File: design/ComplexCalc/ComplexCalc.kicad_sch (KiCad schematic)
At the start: 49 parts, among them J1 V_Battery, J2 Conn_01x09, J3 STLINK, J4 Conn_01x20_Socket, J5 Conn_01x20_Socket, SW1 4, SW10 -, SW11 del, SW12 <-, SW13 7, SW14 8, SW15 9, SW16 M, SW17 SW_DPST_x2, SW18 MOD, SW19 <, SW2 5, SW20 MOD, SW22 ^, SW23 OK, SW24 v, SW26 MOD, SW27 >, SW28 MOD, SW3 6, SW4 1, SW5 2, SW6 3, SW7 =, SW8 ., SW9 0, U2 AMS1117-3.3, U3 STM32F411CEUx, Y1 8MHz

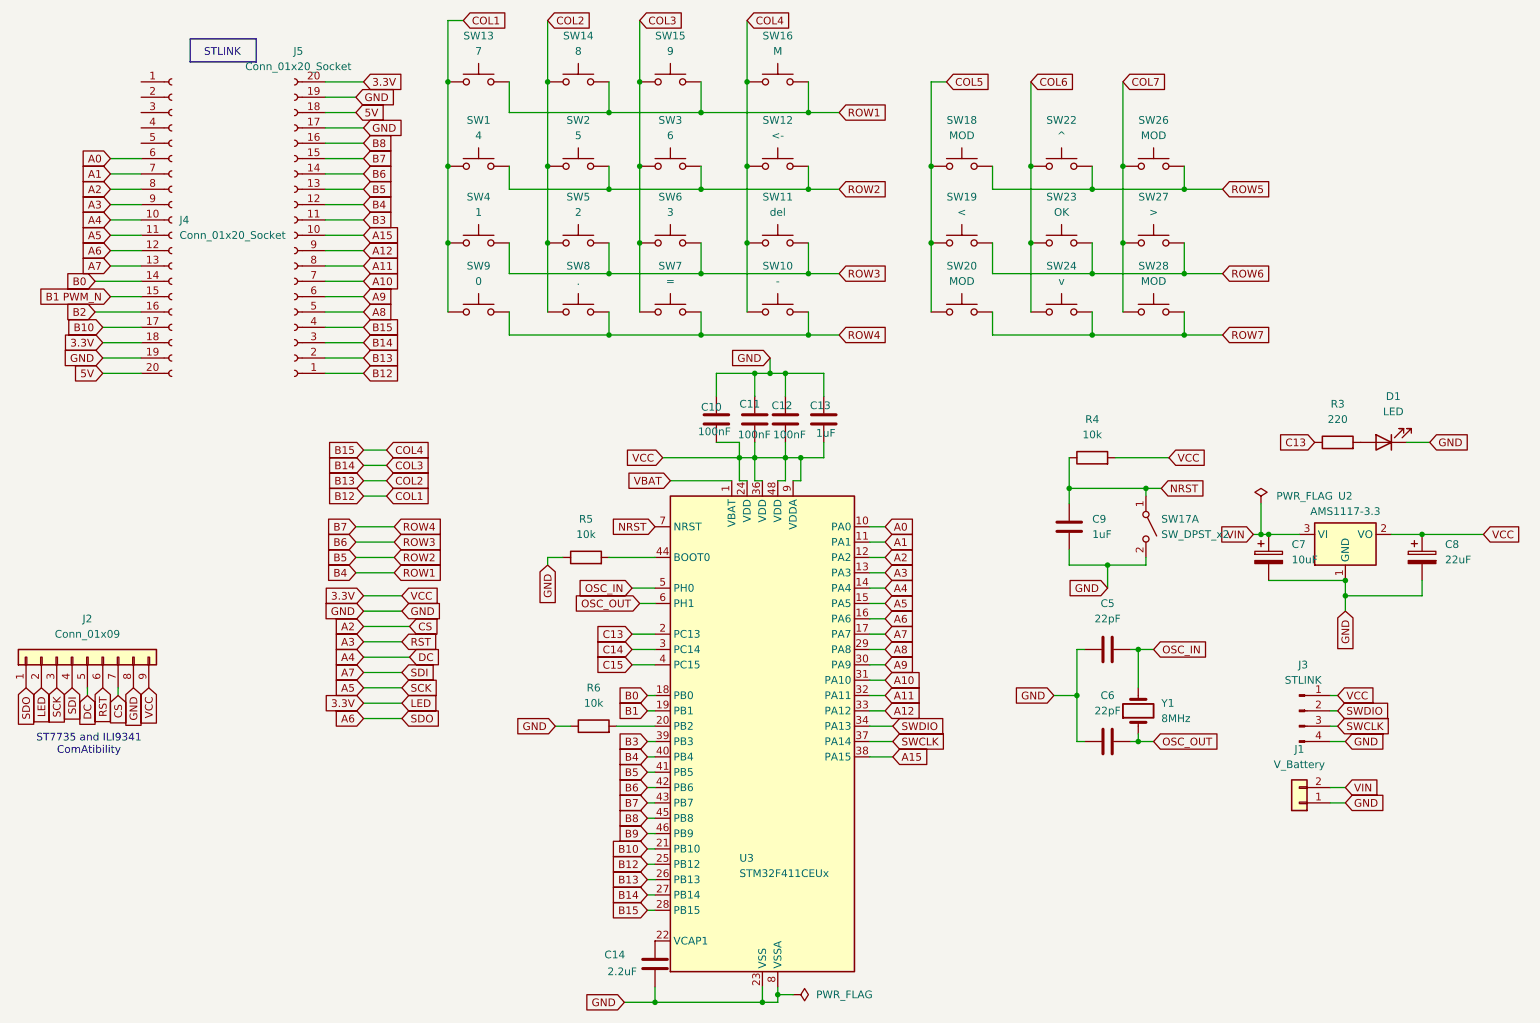
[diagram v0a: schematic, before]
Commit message: Falta conectar algunas cosas y las resistencias con el ADC
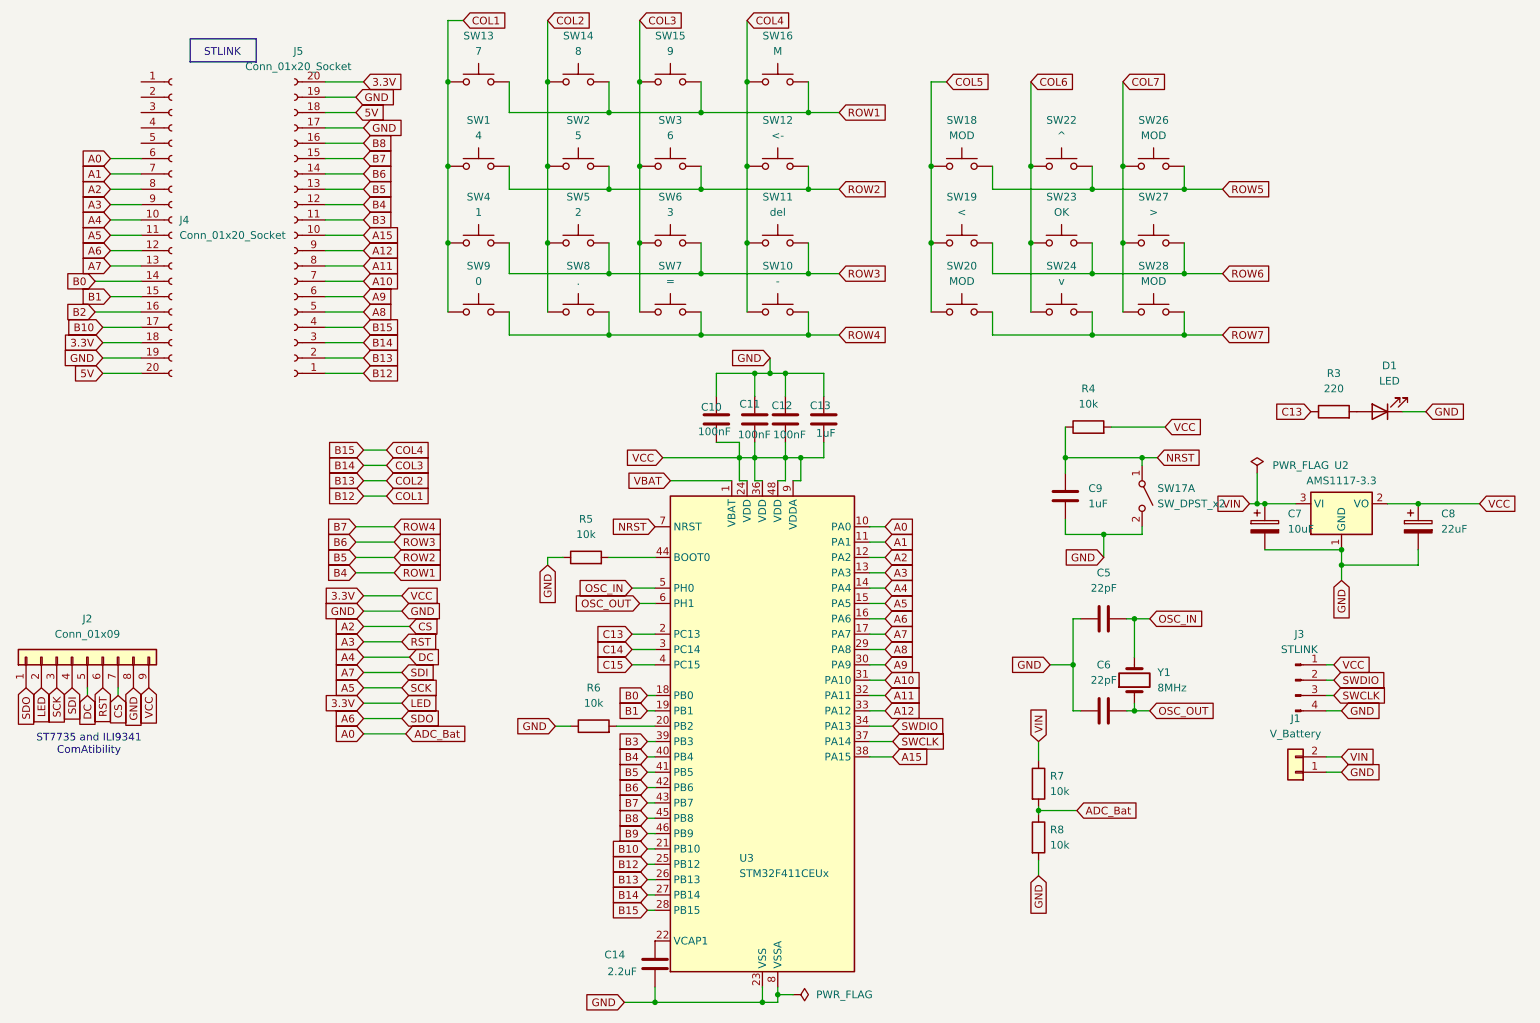
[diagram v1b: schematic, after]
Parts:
- added R7, R8: 10k, Resistor_SMD:R_0805_2012Metric, symbol Device:R
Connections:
- net B1 PWM_N is gone; now on net B1: J4.15 (Pin_15)
- net A0: now also R7.2, R8.1
- net GND: now also R8.2
- net VIN: now also R7.1
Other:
- moved on the sheet: C5, C6, C7, C8, C9, D1, J1, J3, R3, R4, SW17A, U2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

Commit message: Fixxed capacitors values C14,C9 and VBAT to 3.3 V
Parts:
- C14: value 2.2uF -> 4.7uF
- C9: value 1uF -> 100nF
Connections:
- net VBAT is gone; now on net 3.3V: U3.1 (VBAT)
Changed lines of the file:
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@@
 	)
 	(junction
+		(at 144.78 88.9)
+		(diameter 0)
+		(color 0 0 0 0)
+	)
+	(junction
 		(at 114.3 40.64)
 		(diameter 0)
@@
 	(wire
 		(pts
-			(xy 134.62 92.71) (xy 144.78 92.71)
-		)
-		(stroke
-			(width 0)
-			(type default)
-		)
-	)
-	(wire
-		(pts
 			(xy 82.55 105.41) (xy 88.9 105.41)
 		)
@@
 	(wire
 		(pts
-			(xy 133.35 88.9) (xy 146.05 88.9)
+			(xy 133.35 88.9) (xy 144.78 88.9)
 		)
 		(stroke
@@
 	(wire
 		(pts
+			(xy 144.78 88.9) (xy 144.78 92.71)
+		)
+		(stroke
+			(width 0)
+			(type default)
+		)
+	)
+	(wire
+		(pts
 			(xy 180.34 26.67) (xy 177.8 26.67)
 		)
@@
 	(wire
 		(pts
+			(xy 144.78 88.9) (xy 146.05 88.9)
+		)
+		(stroke
+			(width 0)
+			(type default)
+		)
+	)
+	(wire
+		(pts
 			(xy 157.48 26.67) (xy 157.48 31.75)
 		)
@@
 		)
 	)
-	(global_label "VBAT"
-		(shape input)
-		(at 134.62 92.71 180)
-		(fields_autoplaced yes)
-		(effects
-			(font
-				(size 1.27 1.27)
-			)
-			(justify right)
-		)
-		(property "Intersheetrefs" "${INTERSHEET_REFS}"
-			(at 127.22 92.71 0)
-			(hide yes)
-			(show_name no)
-			(do_not_autoplace no)
-			(effects
-				(font
-					(size 1.27 1.27)
-				)
-				(justify right)
-			)
-		)
-	)
 	(global_label "OSC_OUT"
 		(shape input)
@@
 		(fields_autoplaced yes)
 		(property "Reference" "C9"
-			(at 203.835 93.9799 0)
+			(at 203.2 93.9799 0)
 			(show_name no)
 			(do_not_autoplace no)
@@
 			)
 		)
-		(property "Value" "1uF"
-			(at 203.835 96.5199 0)
+		(property "Value" "100nF"
+			(at 203.2 96.5199 0)
 			(show_name no)
 			(do_not_autoplace no)
@@
 			)
 		)
-		(property "Value" "2.2uF"
+		(property "Value" "4.7uF"
 			(at 124.206 173.99 0)
 			(show_name no)

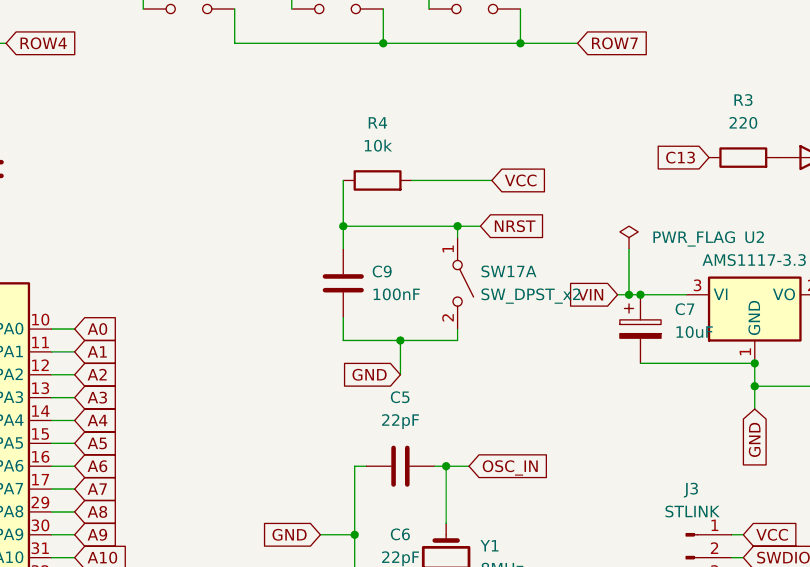
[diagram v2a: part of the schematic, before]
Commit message: ADC trace connected
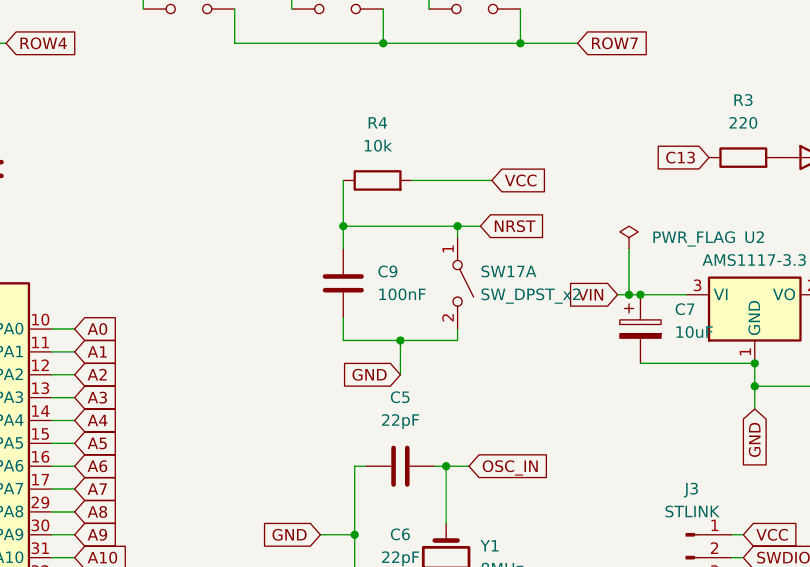
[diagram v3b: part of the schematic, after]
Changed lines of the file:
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@@
 	)
 	(junction
-		(at 144.78 88.9)
+		(at 114.3 40.64)
 		(diameter 0)
 		(color 0 0 0 0)
 	)
 	(junction
-		(at 114.3 40.64)
+		(at 144.78 88.9)
 		(diameter 0)
 		(color 0 0 0 0)
@@
 	(wire
 		(pts
+			(xy 144.78 88.9) (xy 144.78 92.71)
+		)
+		(stroke
+			(width 0)
+			(type default)
+		)
+	)
+	(wire
+		(pts
 			(xy 77.47 46.99) (xy 83.82 46.99)
 		)
@@
 	(wire
 		(pts
-			(xy 144.78 88.9) (xy 144.78 92.71)
-		)
-		(stroke
-			(width 0)
-			(type default)
-		)
-	)
-	(wire
-		(pts
 			(xy 180.34 26.67) (xy 177.8 26.67)
 		)
@@
 	(wire
 		(pts
-			(xy 144.78 88.9) (xy 146.05 88.9)
-		)
-		(stroke
-			(width 0)
-			(type default)
-		)
-	)
-	(wire
-		(pts
 			(xy 157.48 26.67) (xy 157.48 31.75)
 		)
@@
 	(wire
 		(pts
+			(xy 144.78 88.9) (xy 146.05 88.9)
+		)
+		(stroke
+			(width 0)
+			(type default)
+		)
+	)
+	(wire
+		(pts
 			(xy 148.59 74.93) (xy 148.59 78.74)
 		)
@@
 		(fields_autoplaced yes)
 		(property "Reference" "C9"
-			(at 203.2 93.9799 0)
+			(at 203.835 93.9799 0)
 			(show_name no)
 			(do_not_autoplace no)
@@
 		)
 		(property "Value" "100nF"
-			(at 203.2 96.5199 0)
+			(at 203.835 96.5199 0)
 			(show_name no)
 			(do_not_autoplace no)
